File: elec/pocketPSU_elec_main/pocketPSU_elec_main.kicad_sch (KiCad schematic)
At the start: 0 parts

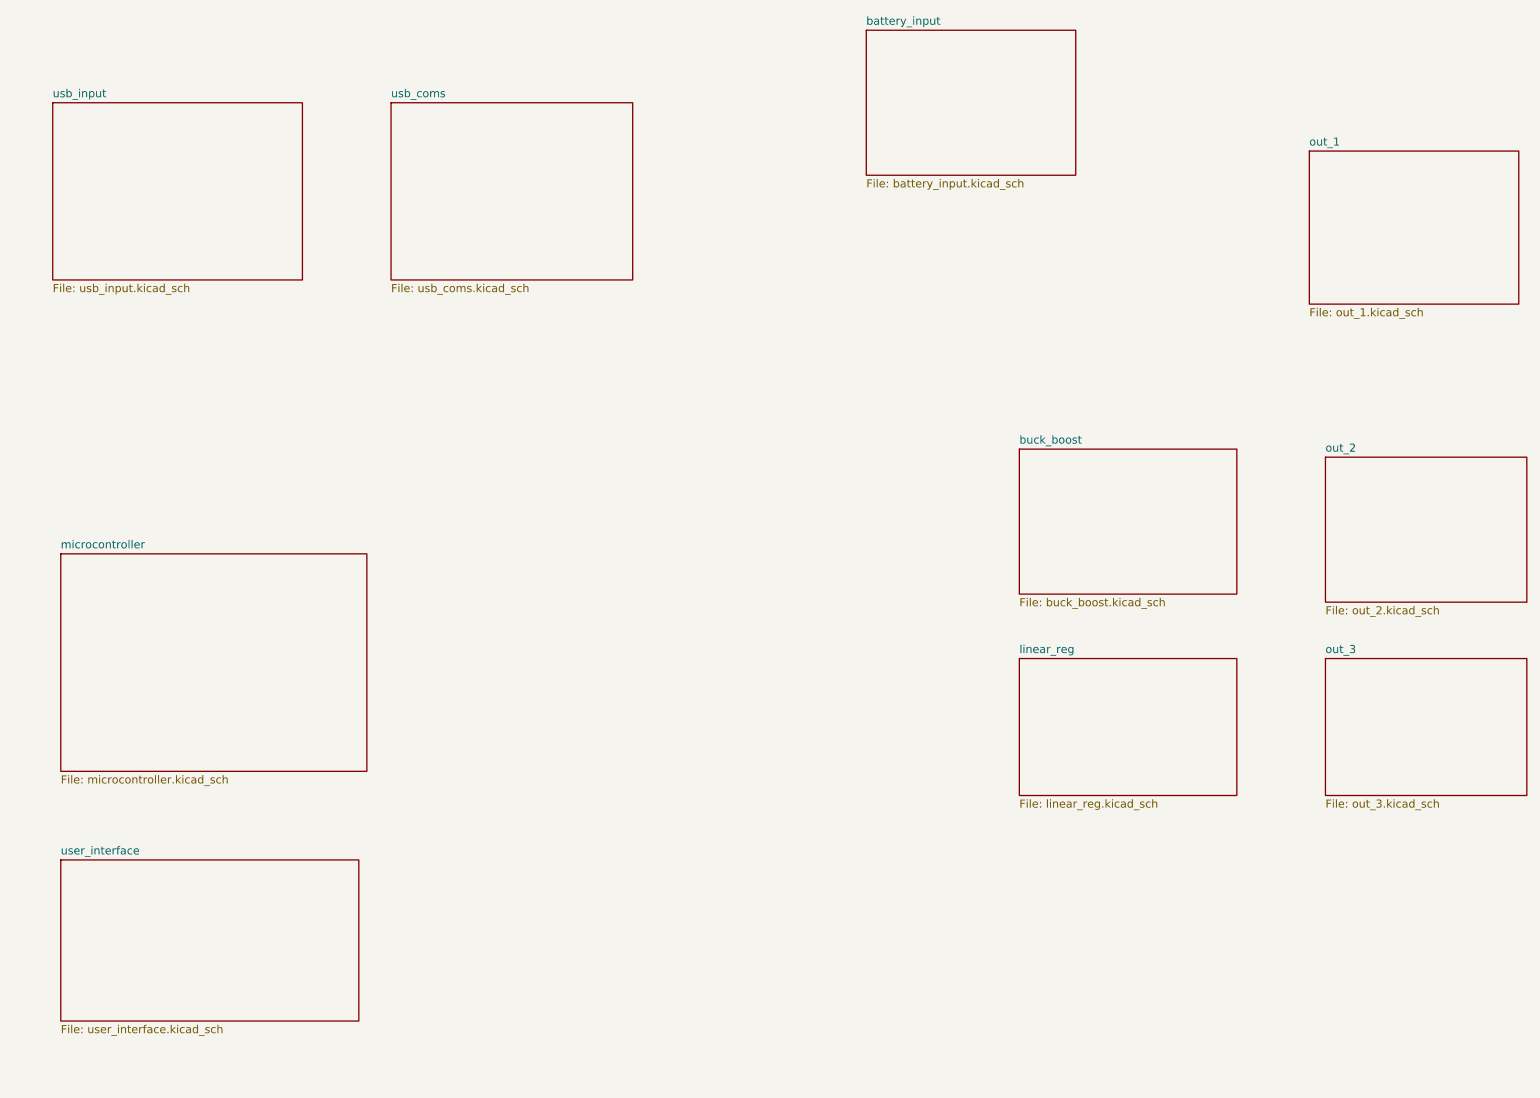
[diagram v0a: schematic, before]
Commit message: added user interface elements
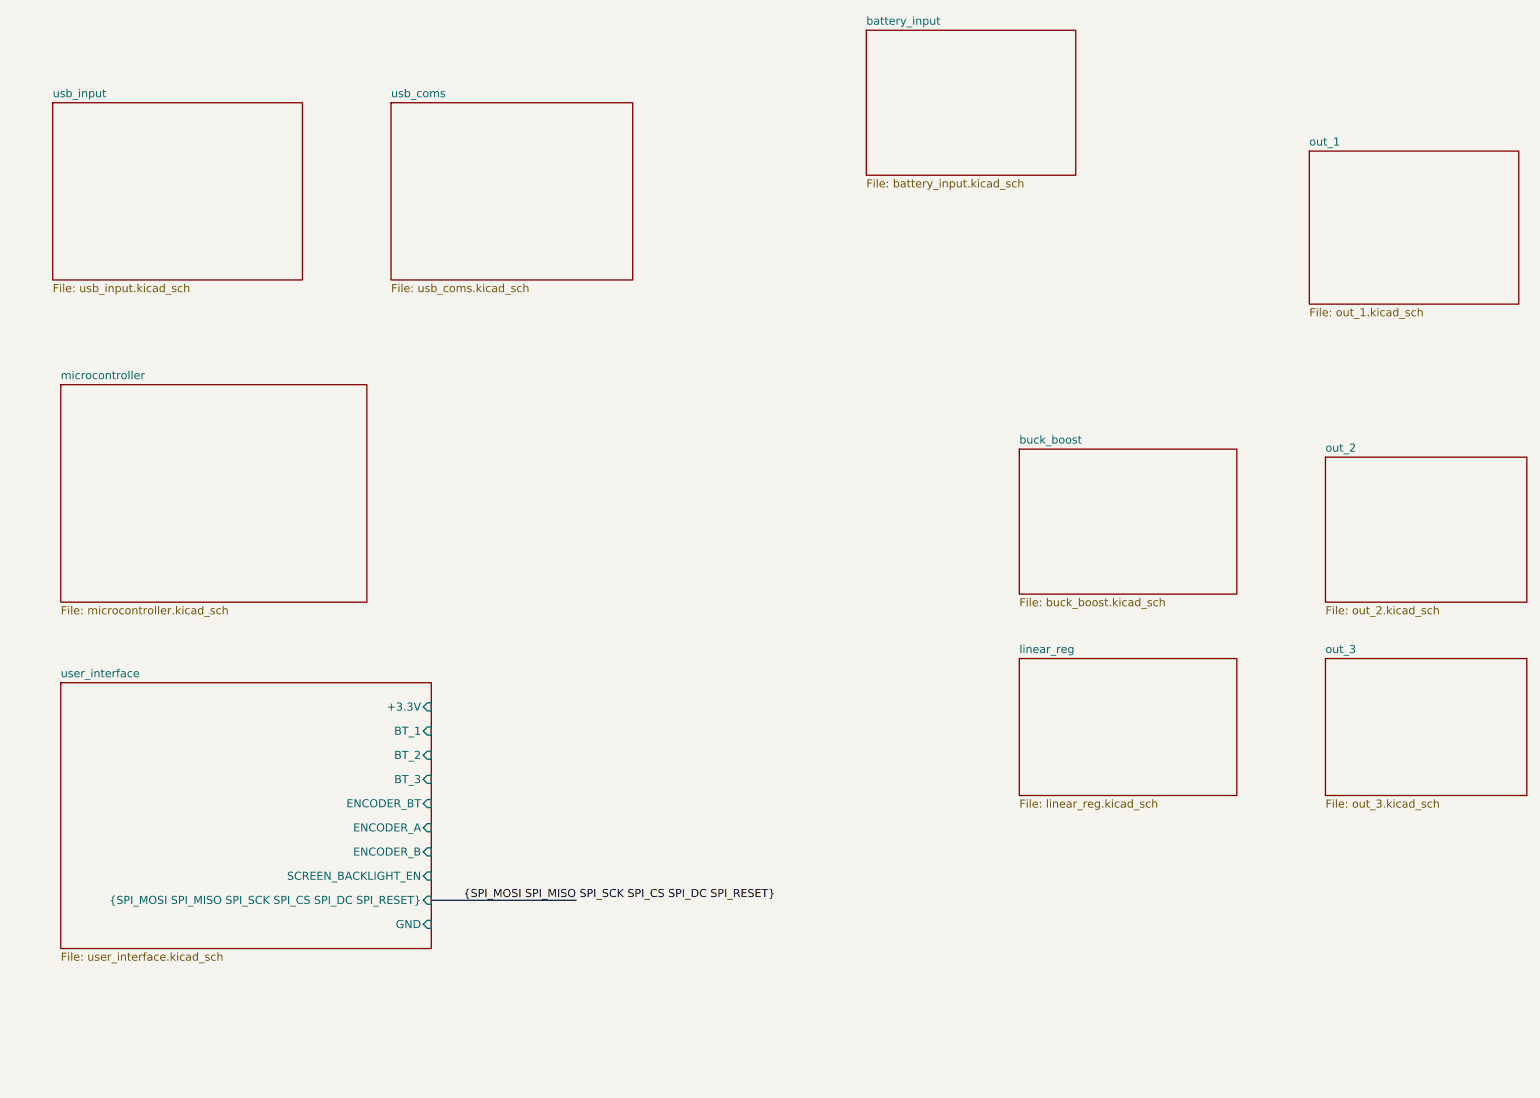
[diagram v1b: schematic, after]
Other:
- sheet user_interface ports: added +3.3V, BT_1, BT_2, BT_3, ENCODER_A, ENCODER_B, ENCODER_BT, GND, SCREEN_BACKLIGHT_EN, {SPI_MOSI SPI_MISO SPI_SCK SPI_CS SPI_DC SPI_RESET}; removed none
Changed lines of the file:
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@@
 	(generator_version "8.0")
 	(paper "A4")
+	(bus
+		(pts
+			(xy 83.82 157.48) (xy 106.68 157.48)
+		)
+		(stroke
+			(width 0)
+			(type default)
+		)
+	)
+	(label "{SPI_MOSI SPI_MISO SPI_SCK SPI_CS SPI_DC SPI_RESET}"
+		(at 88.9 157.48 0)
+		(fields_autoplaced yes)
+		(effects
+			(font
+				(size 1.27 1.27)
+			)
+			(justify left bottom)
+		)
+	)
 	(sheet
 		(at 224.79 119.38)
@@
 	)
 	(sheet
-		(at 25.4 102.87)
+		(at 25.4 76.2)
 		(size 48.26 34.29)
 		(fields_autoplaced yes)
@@
 		)
 		(property "Sheetname" "microcontroller"
-			(at 25.4 102.1584 0)
+			(at 25.4 75.4884 0)
 			(effects
 				(font
@@
 		)
 		(property "Sheetfile" "microcontroller.kicad_sch"
-			(at 25.4 137.7446 0)
+			(at 25.4 111.0746 0)
 			(effects
 				(font
@@
 	)
 	(sheet
-		(at 25.4 151.13)
-		(size 46.99 25.4)
+		(at 25.4 123.19)
+		(size 58.42 41.91)
 		(fields_autoplaced yes)
 		(stroke
@@
 		)
 		(property "Sheetname" "user_interface"
-			(at 25.4 150.4184 0)
+			(at 25.4 122.4784 0)
 			(effects
 				(font
@@
 		)
 		(property "Sheetfile" "user_interface.kicad_sch"
-			(at 25.4 177.1146 0)
-			(effects
-				(font
-					(size 1.27 1.27)
-				)
-				(justify left top)
-			)
-		)
+			(at 25.4 165.6846 0)
+			(effects
+				(font
+					(size 1.27 1.27)
+				)
+				(justify left top)
+			)
+		)
+		(pin "SCREEN_BACKLIGHT_EN" input
+			(at 83.82 153.67 0)
+			(effects
+				(font
+					(size 1.27 1.27)
+				)
+				(justify right)
+			)
+		)
+		(pin "{SPI_MOSI SPI_MISO SPI_SCK SPI_CS SPI_DC SPI_RESET}" input
+			(at 83.82 157.48 0)
+			(effects
+				(font
+					(size 1.27 1.27)
+				)
+				(justify right)
+			)
+		)
+		(pin "GND" input
+			(at 83.82 161.29 0)
+			(effects
+				(font
+					(size 1.27 1.27)
+				)
+				(justify right)
+			)
+		)
+		(pin "+3.3V" input
+			(at 83.82 127 0)
+			(effects
+				(font
+					(size 1.27 1.27)
+				)
+				(justify right)
+			)
+		)
+		(pin "ENCODER_BT" input
+			(at 83.82 142.24 0)
+			(effects
+				(font
+					(size 1.27 1.27)
+				)
+				(justify right)
+			)
+		)
+		(pin "ENCODER_A" input
+			(at 83.82 146.05 0)
+			(effects
+				(font
+					(size 1.27 1.27)
+				)
+				(justify right)
+			)
+		)
+		(pin "BT_3" input
+			(at 83.82 138.43 0)
+			(effects
+				(font
+					(size 1.27 1.27)
+				)
+				(justify right)
+			)
+		)
+		(pin "BT_2" input
+			(at 83.82 134.62 0)
+			(effects
+				(font
+					(size 1.27 1.27)
+				)
+				(justify right)
+			)
+		)
+		(pin "BT_1" input
+			(at 83.82 130.81 0)
+			(effects
+				(font
+					(size 1.27 1.27)
+				)
+				(justify right)
+			)
+		)
+		(pin "ENCODER_B" input
+			(at 83.82 149.86 0)
+			(effects
+				(font
+					(size 1.27 1.27)
+				)
+				(justify right)
+			)
+		)

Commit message: add esp32 micro
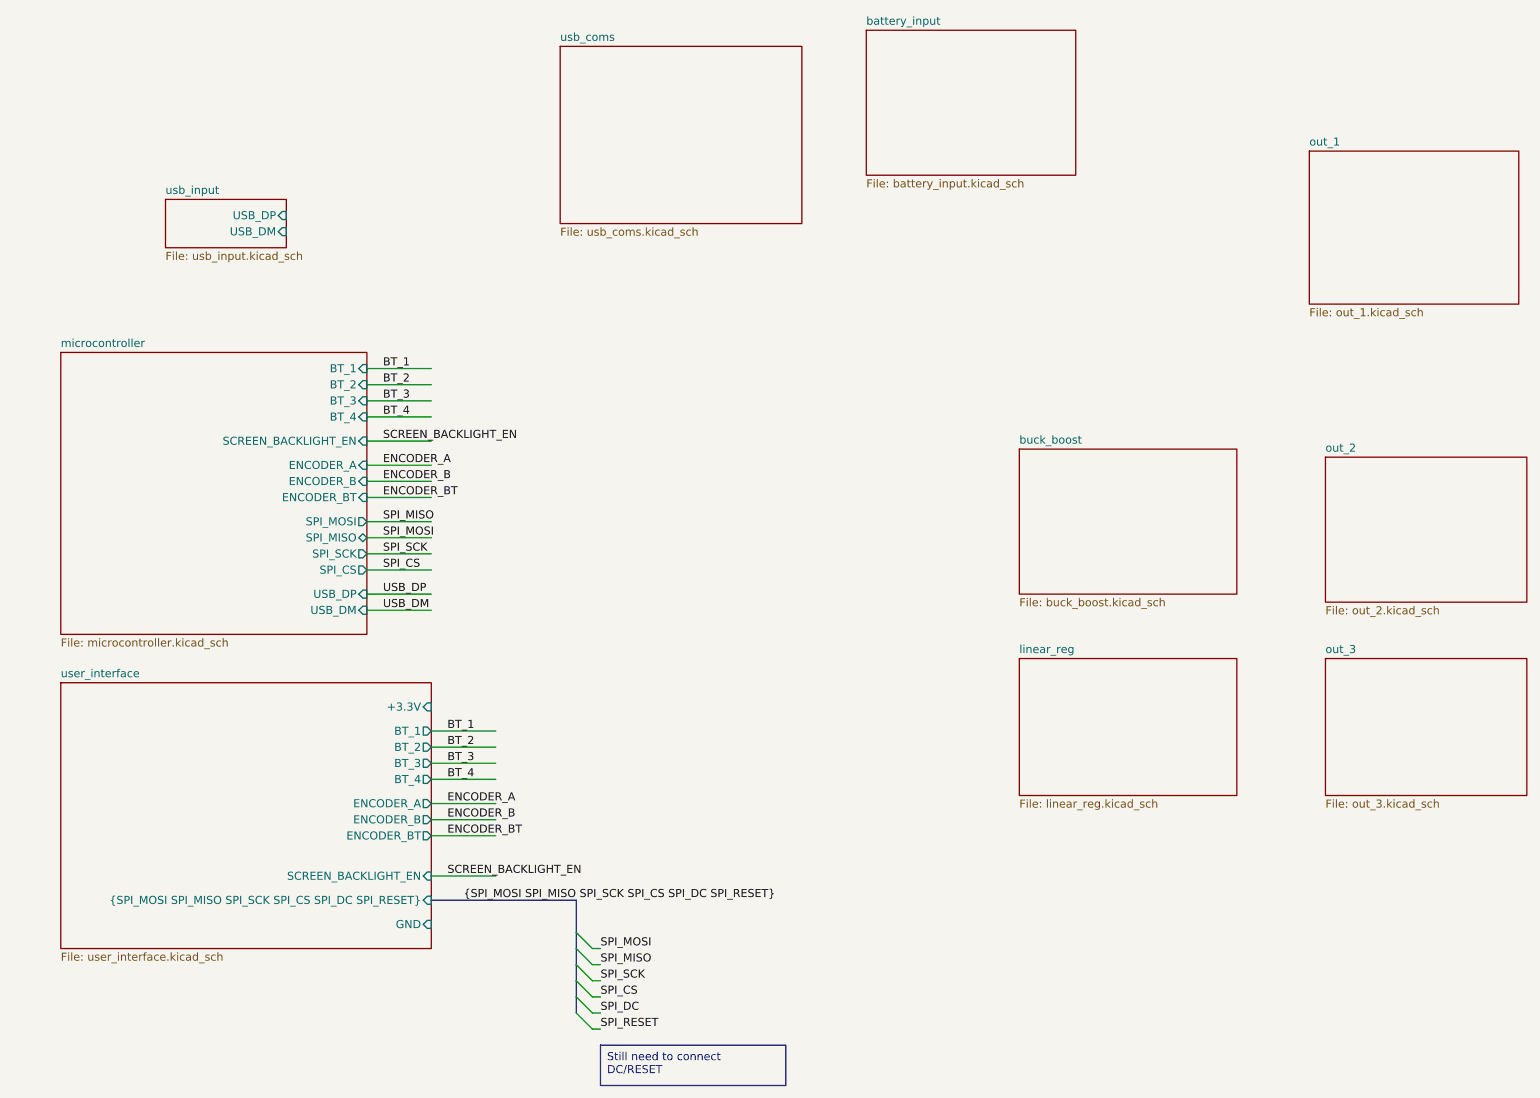
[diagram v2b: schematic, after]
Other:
- sheet microcontroller ports: added BT_1, BT_2, BT_3, BT_4, ENCODER_A, ENCODER_B, ENCODER_BT, SCREEN_BACKLIGHT_EN, SPI_CS, SPI_MISO, SPI_MOSI, SPI_SCK, USB_DM, USB_DP; removed none
- sheet usb_input ports: added USB_DM, USB_DP; removed none
- sheet user_interface ports: added BT_4; removed none

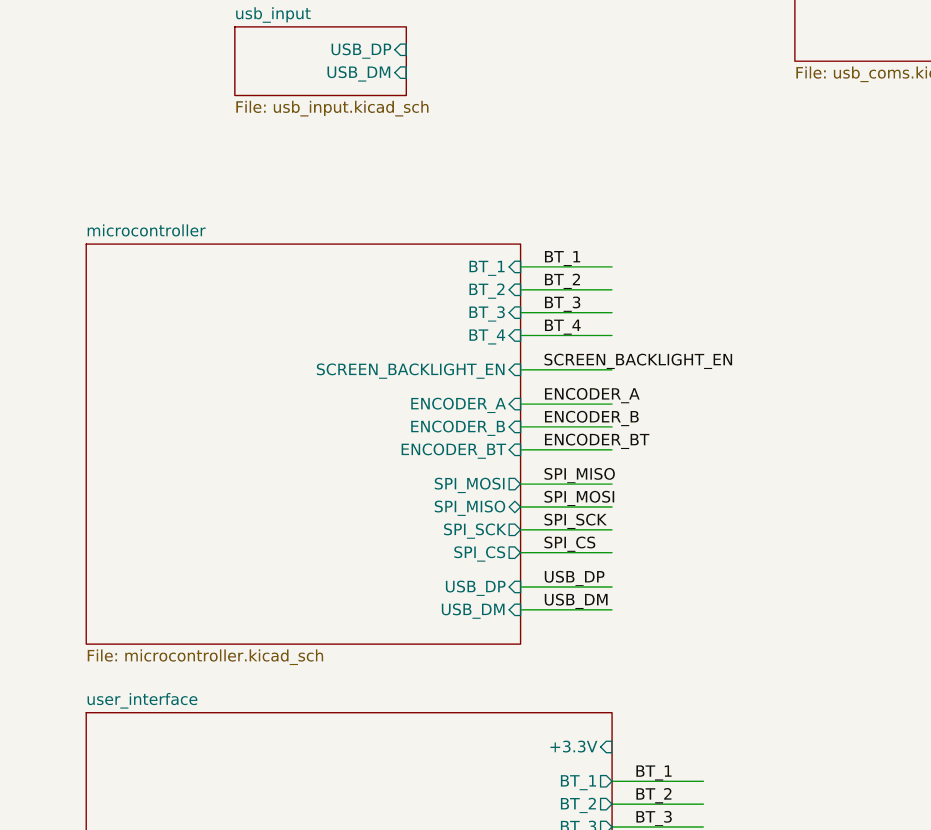
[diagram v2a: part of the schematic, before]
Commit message: Add footprints, change TFT hookup
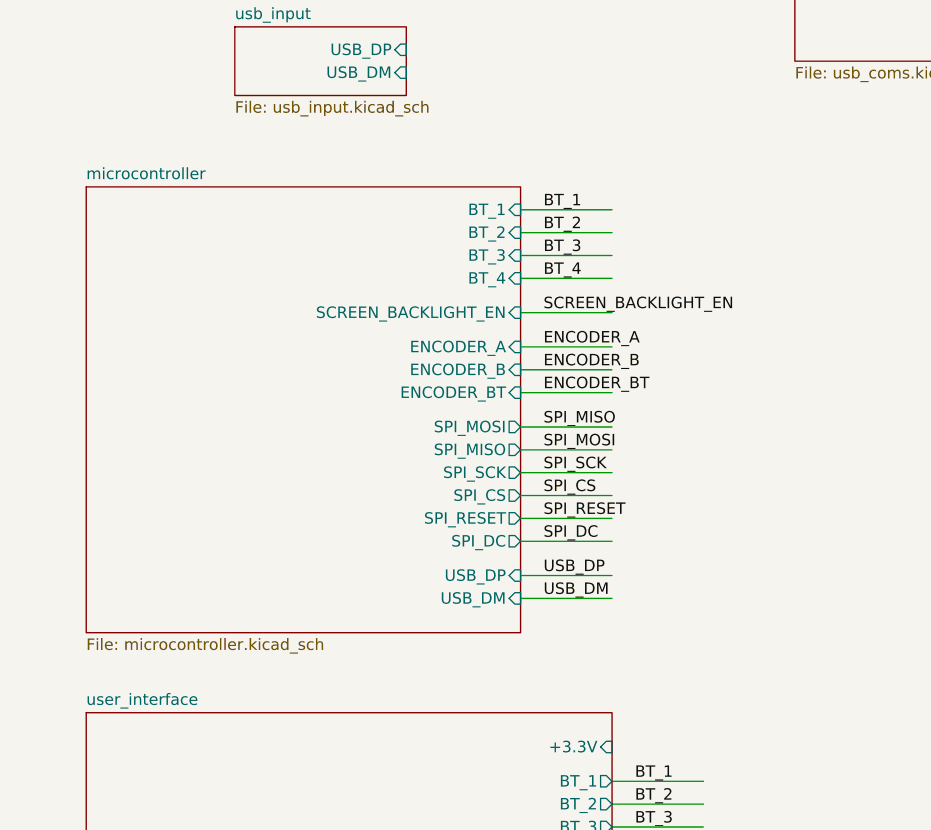
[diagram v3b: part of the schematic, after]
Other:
- sheet microcontroller ports: added SPI_DC, SPI_RESET; removed none
